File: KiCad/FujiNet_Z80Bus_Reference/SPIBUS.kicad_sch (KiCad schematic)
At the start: 19 parts, among them J2 DIAG-ESP_SPI, J3 DIAG-Z80_CONTROL, J4 DIAG-ESP_CONTROL, J5 DIAG-LOCAL_ADD_HIGH, J6 DIAG-LOCAL_ADD_LOW, J7 DIAG-LOCAL_DATA

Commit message: Single PCB layout experiements
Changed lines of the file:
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@@
     (in_bom yes) (on_board yes) (dnp no)
     (property "Reference" "IC?" (at 57.15 35.56 90)
-      (effects (font (size 1.4986 1.4986)) (justify left bottom))
+      (effects (font (size 1.5 1.5)))
     )
     (property "Value" "74595N" (at 48.26 50.8 0)
@@
         )
         (path "/532c0392-800e-45cc-8170-6d32f2390e83/00000000-0000-0000-0000-000068f578e9/00000000-0000-0000-0000-000068fd7452"
-          (reference "IC8") (unit 1)
+          (reference "SPI-LOCAL_DATA.OUT1") (unit 1)
         )
       )
@@
     (in_bom yes) (on_board yes) (dnp no)
     (property "Reference" "IC?" (at 57.15 139.7 90)
-      (effects (font (size 1.4986 1.4986)) (justify left bottom))
+      (effects (font (size 1.4986 1.4986)))
     )
     (property "Value" "74595N" (at 48.26 153.67 0)
@@
         )
         (path "/532c0392-800e-45cc-8170-6d32f2390e83/00000000-0000-0000-0000-000068f578e9/00000000-0000-0000-0000-000068fd7452"
-          (reference "IC10") (unit 1)
+          (reference "SPI-LOCAL_ADD_L.OUT1") (unit 1)
         )
       )
@@
     (in_bom yes) (on_board yes) (dnp no)
     (property "Reference" "IC?" (at 57.15 171.45 90)
-      (effects (font (size 1.4986 1.4986)) (justify left bottom))
+      (effects (font (size 1.4986 1.4986)))
     )
     (property "Value" "74595N" (at 48.26 186.69 0)
@@
         )
         (path "/532c0392-800e-45cc-8170-6d32f2390e83/00000000-0000-0000-0000-000068f578e9/00000000-0000-0000-0000-000068fd7452"
-          (reference "IC11") (unit 1)
+          (reference "SPI-LOCAL_ADD_HIGH.OUT1") (unit 1)
         )
       )
@@
   (symbol (lib_id "FujiNet_Z80Bus_Reference-rescue:74165N-Z80ESP-eagle-import") (at 154.94 34.29 0) (unit 1)
     (in_bom yes) (on_board yes) (dnp no)
-    (property "Reference" "IC?" (at 154.305 34.925 0)
-      (effects (font (size 1.4986 1.4986)) (justify left bottom))
+    (property "Reference" "IC?" (at 154.305 34.925 90)
+      (effects (font (size 1.4986 1.4986)))
     )
     (property "Value" "74165N" (at 147.32 54.61 0)
@@
         )
         (path "/532c0392-800e-45cc-8170-6d32f2390e83/00000000-0000-0000-0000-000068f578e9/00000000-0000-0000-0000-000068fd7452"
-          (reference "IC16") (unit 1)
+          (reference "SPI-LOCAL_DATA.IN1") (unit 1)
         )
       )
@@
   (symbol (lib_id "FujiNet_Z80Bus_Reference-rescue:74165N-Z80ESP-eagle-import") (at 154.94 74.93 0) (unit 1)
     (in_bom yes) (on_board yes) (dnp no)
-    (property "Reference" "IC?" (at 154.305 75.565 0)
-      (effects (font (size 1.4986 1.4986)) (justify left bottom))
+    (property "Reference" "IC?" (at 154.305 75.565 90)
+      (effects (font (size 1.4986 1.4986)))
     )
     (property "Value" "74165N" (at 147.32 95.25 0)
@@
         )
         (path "/532c0392-800e-45cc-8170-6d32f2390e83/00000000-0000-0000-0000-000068f578e9/00000000-0000-0000-0000-000068fd7452"
-          (reference "IC17") (unit 1)
+          (reference "SPI-Z80_CONTROL.IN1") (unit 1)
         )
       )
@@
   (symbol (lib_id "FujiNet_Z80Bus_Reference-rescue:74165N-Z80ESP-eagle-import") (at 142.24 138.43 0) (unit 1)
     (in_bom yes) (on_board yes) (dnp no)
-    (property "Reference" "IC?" (at 141.605 139.065 0)
-      (effects (font (size 1.4986 1.4986)) (justify left bottom))
+    (property "Reference" "IC?" (at 141.605 139.065 90)
+      (effects (font (size 1.4986 1.4986)))
     )
     (property "Value" "74165N" (at 134.62 158.75 0)
@@
         )
         (path "/532c0392-800e-45cc-8170-6d32f2390e83/00000000-0000-0000-0000-000068f578e9/00000000-0000-0000-0000-000068fd7452"
-          (reference "IC12") (unit 1)
+          (reference "SPI-LOCAL_ADDR_L.IN1") (unit 1)
         )
       )
@@
   (symbol (lib_id "FujiNet_Z80Bus_Reference-rescue:74165N-Z80ESP-eagle-import") (at 142.24 179.07 0) (unit 1)
     (in_bom yes) (on_board yes) (dnp no)
-    (property "Reference" "IC?" (at 141.605 179.705 0)
-      (effects (font (size 1.4986 1.4986)) (justify left bottom))
+    (property "Reference" "IC?" (at 141.605 179.705 90)
+      (effects (font (size 1.4986 1.4986)))
     )
     (property "Value" "74165N" (at 134.62 199.39 0)
@@
         )
         (path "/532c0392-800e-45cc-8170-6d32f2390e83/00000000-0000-0000-0000-000068f578e9/00000000-0000-0000-0000-000068fd7452"
-          (reference "IC14") (unit 1)
+          (reference "SPI-LOCAL_ADD_H.IN1") (unit 1)
         )
       )
@@
         )
         (path "/532c0392-800e-45cc-8170-6d32f2390e83/00000000-0000-0000-0000-000068f578e9/00000000-0000-0000-0000-000068fd7452"
-          (reference "RN2") (unit 1)
+          (reference "LOCAL_DATA_BIAS1") (unit 1)
         )
       )
@@
         )
         (path "/532c0392-800e-45cc-8170-6d32f2390e83/00000000-0000-0000-0000-000068f578e9/00000000-0000-0000-0000-000068fd7452"
-          (reference "RN3") (unit 1)
+          (reference "ESP_CONTROL_BIAS1") (unit 1)
         )
       )
@@
     (in_bom yes) (on_board yes) (dnp no)
     (property "Reference" "IC?" (at 57.15 85.09 90)
-      (effects (font (size 1.4986 1.4986)) (justify left bottom))
+      (effects (font (size 1.4986 1.4986)))
     )
     (property "Value" "74595N" (at 48.26 100.33 0)
@@
         )
         (path "/532c0392-800e-45cc-8170-6d32f2390e83/00000000-0000-0000-0000-000068f578e9/00000000-0000-0000-0000-000068fd7452"
-          (reference "IC9") (unit 1)
-        )
-      )
+          (reference "SPI-ESP_CONTROL.OUT1") (unit 1)
+        )
+      )

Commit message: Massive fix to KiCad Labels
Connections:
- net ESP_CONTROL_BUSRQ renamed ESP_CONTROL.BUSRQ
- net ESP_CONTROL_IORQ renamed ESP_CONTROL.IORQ
- net ESP_CONTROL.IORQ: now also RN?.4; no longer RN?.5
- net ESP_CONTROL_MEMRQ renamed ESP_CONTROL.MEMRQ
- net ESP_CONTROL.MEMRQ: now also RN?.5; no longer RN?.4
- net ESP_CONTROL_NMI renamed ESP_CONTROL.NMI
- net ESP_CONTROL_RD renamed ESP_CONTROL.RD
- net ESP_CONTROL_ROMCS renamed ESP_CONTROL.ROMCS
- net ESP_CONTROL_WAIT renamed ESP_CONTROL.WAIT
- net ESP_CONTROL_WR renamed ESP_CONTROL.WR
- net ESP_SPI.CE renamed ESP_SPI_INT.CE
- net ESP_SPI.MISO renamed ESP_SPI_INT.MISO
- net ESP_SPI.MOSI renamed ESP_SPI_INT.MOSI
- net ESP_SPI.MR renamed ESP_SPI_INT.MR
- net ESP_SPI.OE renamed ESP_SPI_INT.OE
- net ESP_SPI.PL renamed ESP_SPI_INT.PL
- net ESP_SPI.SCK renamed ESP_SPI_INT.SCK
- net ESP_SPI.STC renamed ESP_SPI_INT.STC
- net LOCAL_ADD_0 renamed LOCAL_A0
- net LOCAL_ADD_1 renamed LOCAL_A1
- net LOCAL_ADD_10 renamed LOCAL_A10
- net LOCAL_ADD_11 renamed LOCAL_A11
- net LOCAL_ADD_12 renamed LOCAL_A12
- net LOCAL_ADD_13 renamed LOCAL_A13
- net LOCAL_ADD_14 renamed LOCAL_A14
- net LOCAL_ADD_15 renamed LOCAL_A15
- net LOCAL_ADD_2 renamed LOCAL_A2
- net LOCAL_ADD_3 renamed LOCAL_A3
- net LOCAL_ADD_4 renamed LOCAL_A4
- net LOCAL_ADD_5 renamed LOCAL_A5
- net LOCAL_ADD_6 renamed LOCAL_A6
- net LOCAL_ADD_7 renamed LOCAL_A7
- net LOCAL_ADD_8 renamed LOCAL_A8
- net LOCAL_ADD_9 renamed LOCAL_A9
- net LOCAL_DATA_0 renamed LOCAL_D0
- net LOCAL_DATA_1 renamed LOCAL_D1
- net LOCAL_DATA_2 renamed LOCAL_D2
- net LOCAL_DATA_3 renamed LOCAL_D3
- net LOCAL_DATA_4 renamed LOCAL_D4
- net LOCAL_DATA_5 renamed LOCAL_D5
- net LOCAL_DATA_6 renamed LOCAL_D6
- net LOCAL_DATA_7 renamed LOCAL_D7
- net VCC renamed +5V
- net Z80_BUSACK renamed Z80_CONTROL.BUSACK
- net Z80_BUSRQ renamed Z80_CONTROL.BUSRQ
- net Z80_IORQ renamed Z80_CONTROL.IORQ
- net Z80_MEMRQ renamed Z80_CONTROL.MEMRQ
- net Z80_NMI renamed Z80_CONTROL.NMI
- net Z80_RD renamed Z80_CONTROL.RD
- net Z80_WAIT renamed Z80_CONTROL.WAIT
- net Z80_WR renamed Z80_CONTROL.WR
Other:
- moved on the sheet: D?, IC?A, J2, J3, J4, J5, J6, J7, RN?

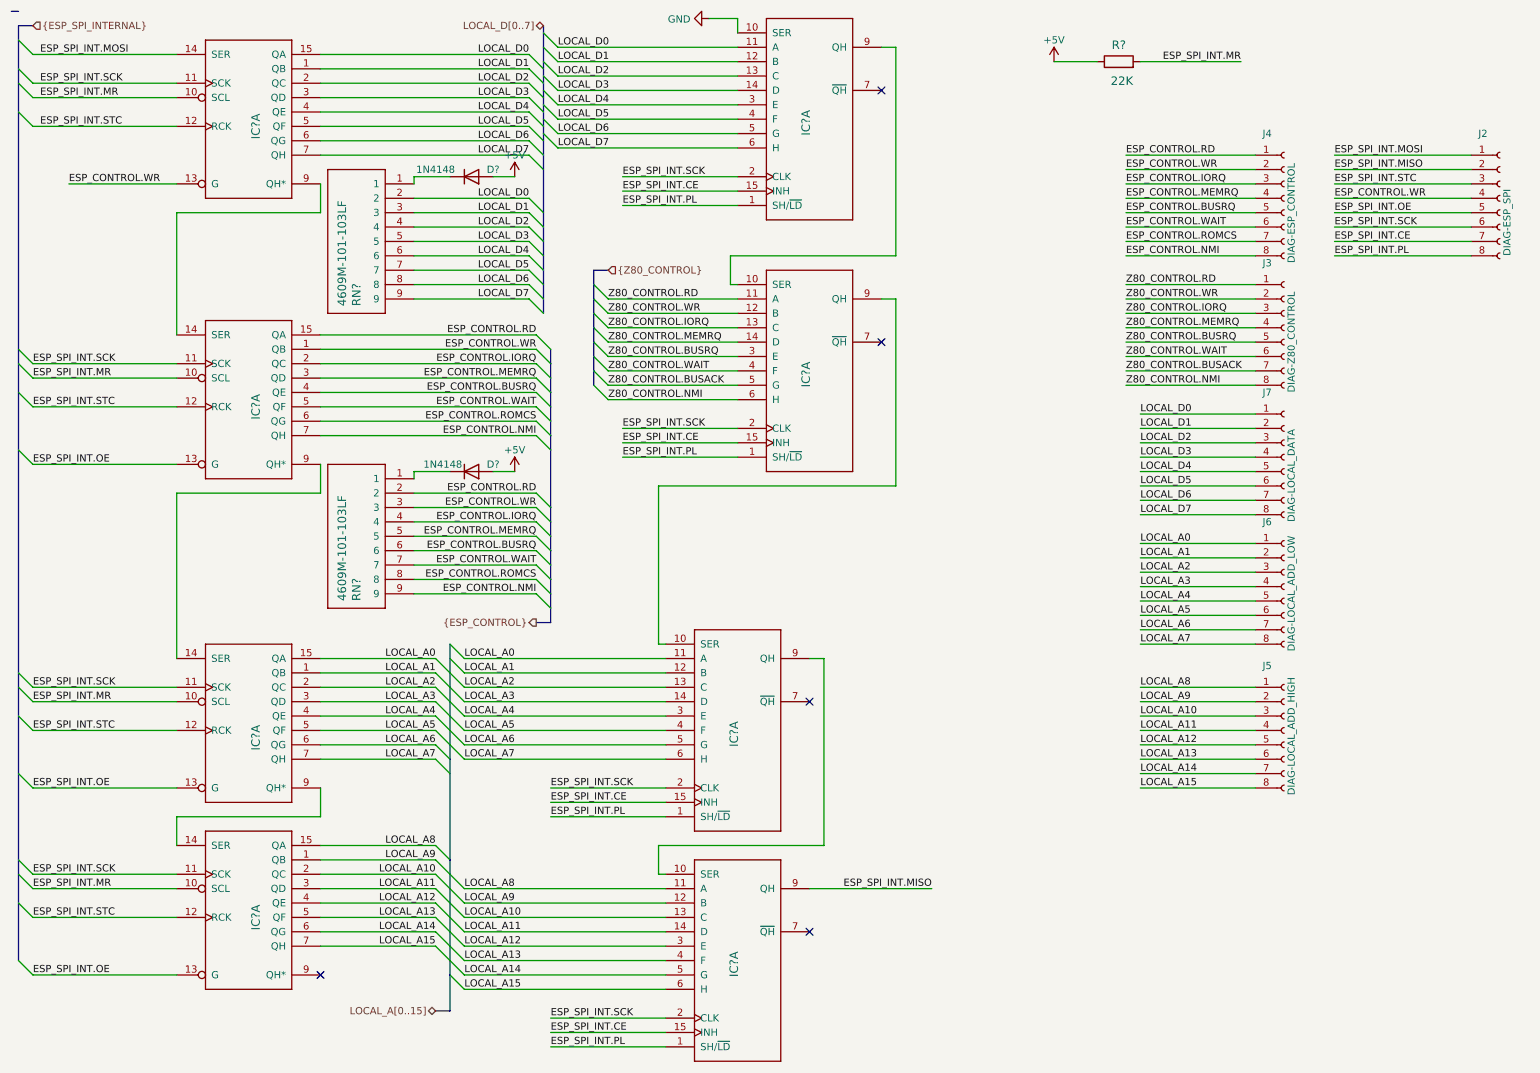
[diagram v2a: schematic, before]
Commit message: KiCad Labels mostly fixed
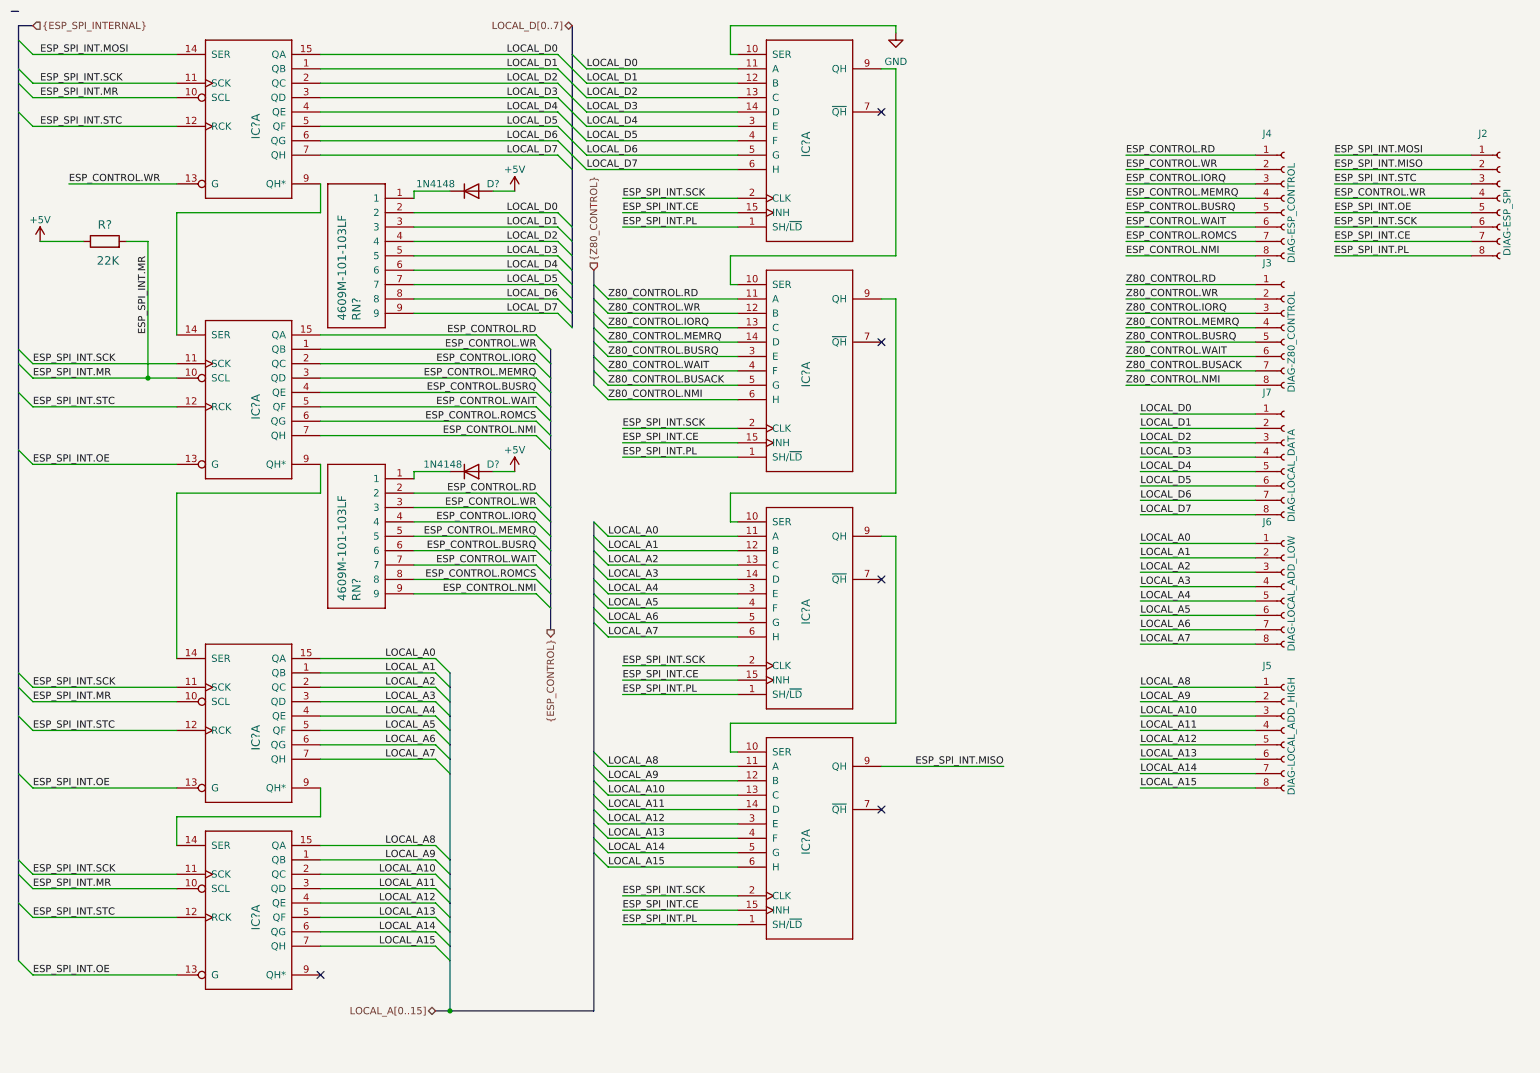
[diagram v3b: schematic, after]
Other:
- moved on the sheet: D?, IC?A, R?, RN?
